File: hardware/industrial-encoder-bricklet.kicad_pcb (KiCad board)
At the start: 2 copper layers, 40 x 40 mm, 67 parts, among them P1 CON-SENSOR, P2 Boot, P3 CONN_8, U1 XMC1XXX24, U2 OPA358, U3 ISL32173E, U4 DRILL, U5 DRILL, U6 DRILL, U7 DRILL

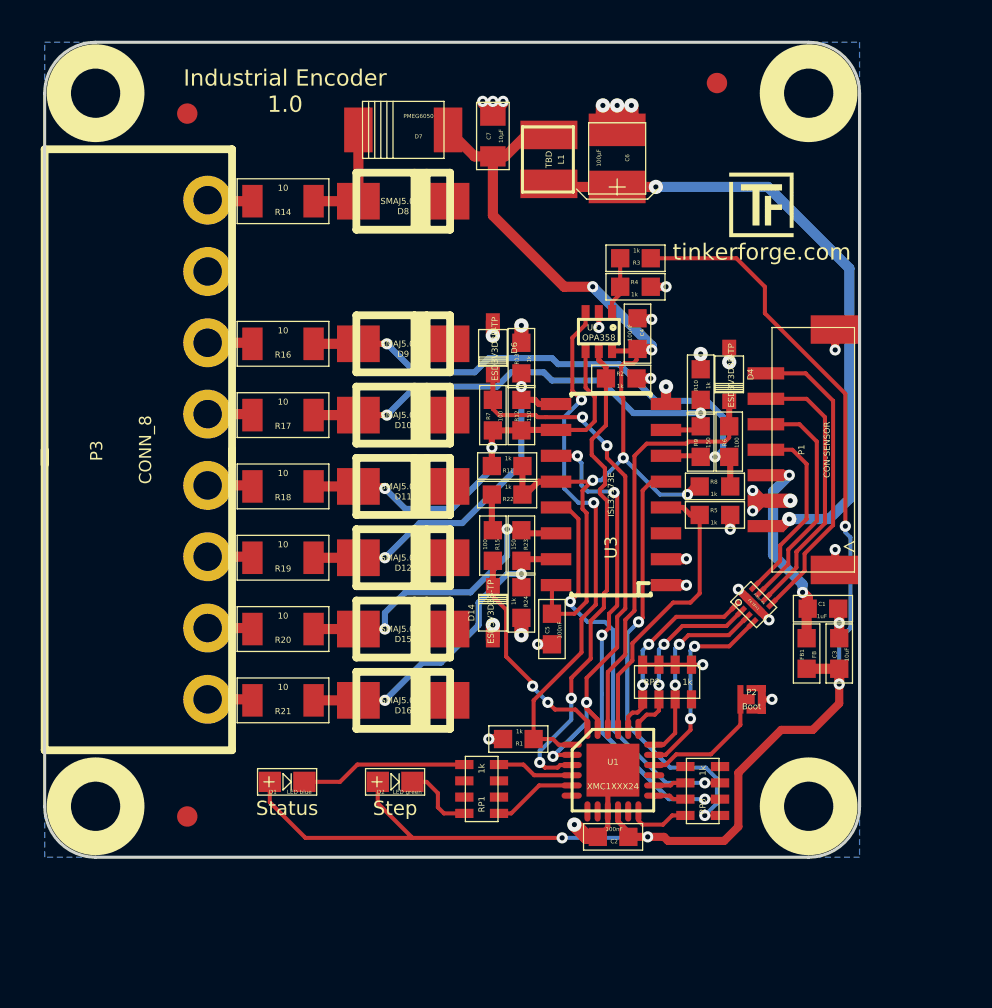
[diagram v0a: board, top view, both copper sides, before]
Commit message: fix filter circuit, not completly finished
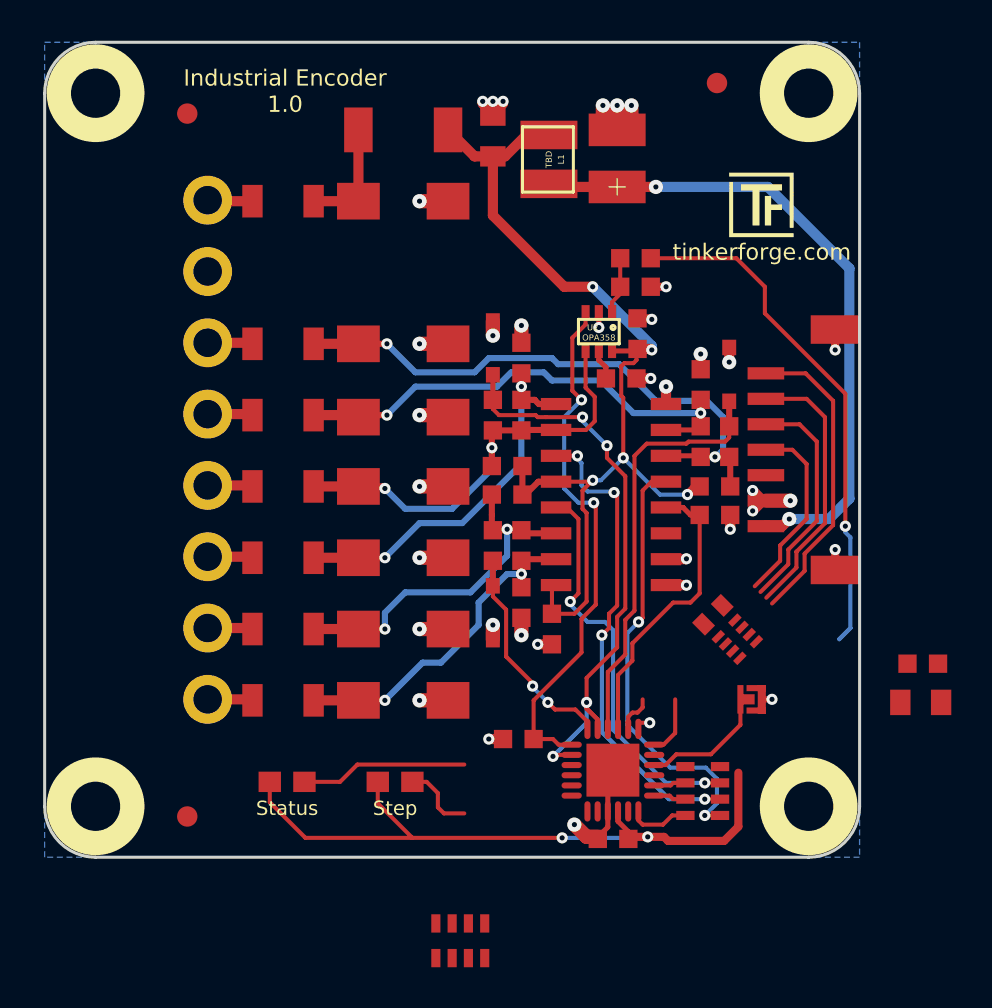
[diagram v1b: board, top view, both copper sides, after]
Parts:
- removed D14: ESD3V3D3B-TP, SOD-323
- removed D15, D16: SMAJ5.0CA, DO-214AC
- removed FB1: FB, kicad-libraries:0603F
- removed FILTER1: Filter-4x, kicad-libraries:DFN8-17x135
- added C8: 10µF, kicad-libraries:C0805, F.Cu at (188.4, 90.5)
- added D13: SMAJ5.0CA, DO-214AC, F.Cu at (184.0, 118.2)
- added D3: ESD3V3D3B-TP, SOD-323, F.Cu at (200.0, 102.2)
- added D5: PMEG6050, SOD-128, F.Cu at (184.0, 90.2)
- C1: value 1uF -> TBD; footprint kicad-libraries:0603F -> kicad-libraries:C0402E
- C2: value 100nF -> 10uF; footprint kicad-libraries:0603F -> kicad-libraries:C0805
- C3: value 10uF -> 100nF; footprint kicad-libraries:0603F -> kicad-libraries:C0603F
- C4: value 100nF -> 1uF; footprint kicad-libraries:0603F -> kicad-libraries:C0603F
- C5: footprint kicad-libraries:0603F -> kicad-libraries:C0603F
- C6: value 100µF -> 100nF; footprint 3528-21 -> kicad-libraries:C0603F
- C7: value 10µF -> 100µF; footprint kicad-libraries:0805 -> 3528-21
- D11: value SMAJ5.0CA -> ESD3V3D3B-TP; footprint DO-214AC -> SOD-323
- D6: value ESD3V3D3B-TP -> SMAJ5.0CA; footprint SOD-323 -> DO-214AC
- D7: value PMEG6050 -> SMAJ5.0CA; footprint SOD-128 -> DO-214AC
- R1, R10, R11, R12, R13, R15, R2, R22, R23, R24, R3, R4, R5, R6, R7, R8, R9: footprint 0603F -> R0603F
- R14, R16, R17, R18, R19, R20, R21: footprint 1206 -> R1206
- RP1: value 1k -> TBD; footprint kicad-libraries:0603X4 -> 4X0402
- RP2: footprint 0603X4 -> kicad-libraries:0603X4
- moved C6 23.3 mm to (191.3, 114.7), turned to 270 degrees
- moved C4 21.4 mm to (209.5, 116.4), turned to 180 degrees
- moved C2 16.5 mm to (209.4, 118.3), turned to 180 degrees
- moved RP2 16.3 mm to (186.8, 130.0)
- moved C5 15.1 mm to (195.5, 100.2), turned to 90 degrees
- moved RP1 14.5 mm to (200.4, 115.2), turned to 135 degrees
- moved C3 14.4 mm to (194.3, 125.0), turned to 0 degrees
- moved D4 11.7 mm to (188.4, 100.9)
- moved D8 10.6 mm to (184.0, 104.3)
- moved D7 10.5 mm to (184.0, 100.7)
- moved D6 8.44 mm to (184.0, 93.7), turned to 0 degrees
- moved D11 7.60 mm to (188.4, 113.9), turned to 90 degrees
- moved D10 7.00 mm to (184.0, 111.2)
- moved D9 7.00 mm to (184.0, 107.7)
- moved C7 6.20 mm to (194.5, 91.6), turned to 90 degrees
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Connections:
- C4 pad 1: +5VA -> GND
- C4 pad 2: GND -> VCC
- C6 pad 1: +5V -> +5VA
- C7 pad 1: GND -> +5V
- C7 pad 2: +5VA -> GND
- D10 pad 1: ~A -> ~B
- D11 pad 1: B/CLK -> GND
- D11 pad 2: GND -> I-T
- D12 pad 1: ~B -> I
- D4 pad 2: A-T -> B-T
- D6 pad 1: GND -> Net-(D5-Pad2)
- D6 pad 2: B-T -> GND
- D7 pad 1: +5VA -> A/DAT
- D7 pad 2: Net-(D7-Pad2) -> GND
- D8 pad 1: Net-(D7-Pad2) -> ~A
- D9 pad 1: A/DAT -> B/CLK
- P1 pad 3: Net-(C1-Pad2) -> VCC
- P1 pad 4: Net-(FILTER1-Pad8) -> Net-(P1-Pad4)
- P1 pad 5: Net-(FILTER1-Pad7) -> Net-(P1-Pad5)
- P1 pad 6: Net-(FILTER1-Pad6) -> Net-(P1-Pad6)
- P1 pad 7: Net-(FILTER1-Pad5) -> Net-(C1-Pad2)
- R14 pad 2: Net-(D7-Pad2) -> Net-(D5-Pad2)
- RP1 pad 1: Net-(D1-Pad2) -> S-CS
- RP1 pad 2: (no net) -> S-CLK
- RP1 pad 3: (no net) -> S-MOSI
- RP1 pad 4: Net-(D2-Pad2) -> S-MISO
- RP1 pad 5: Net-(RP1-Pad5) -> Net-(C1-Pad2)
- RP1 pad 6: (no net) -> Net-(P1-Pad6)
- RP1 pad 7: (no net) -> Net-(P1-Pad5)
- RP1 pad 8: Net-(RP1-Pad8) -> Net-(P1-Pad4)
- RP2 pad 1: GND -> Net-(D1-Pad2)
- RP2 pad 2: GND -> (no net)
- RP2 pad 3: GND -> (no net)
- RP2 pad 4: GND -> Net-(D2-Pad2)
- RP2 pad 5: S-CS -> Net-(RP2-Pad5)
- RP2 pad 6: S-CLK -> (no net)
- RP2 pad 7: S-MOSI -> (no net)
- RP2 pad 8: (no net) -> Net-(RP2-Pad8)
- U1 pad 11: (no net) -> S-CLK
- U1 pad 19: S-CLK -> B-CLK-EN
- U1 pad 3: B-CLK-EN -> (no net)
- U1 pad 4: Net-(RP1-Pad8) -> (no net)
- U1 pad 5: Net-(RP1-Pad5) -> (no net)
- U1 pad 7: (no net) -> Net-(RP2-Pad8)
- U1 pad 8: (no net) -> Net-(RP2-Pad5)
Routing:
- net B-CLK-EN: track 24.3 -> 2.61 mm, vias 2 -> 1
- net Net-(FILTER1-Pad5): track 15.0 -> 0.00 mm
- net Net-(P1-Pad6): track 0.00 -> 13.3 mm
- net Net-(FILTER1-Pad6): track 13.3 -> 0.00 mm
- net VCC: track 72.0 -> 60.1 mm, vias 4 -> 3
- net Net-(P1-Pad5): track 0.00 -> 11.4 mm
- net Net-(FILTER1-Pad7): track 11.4 -> 0.00 mm
- net S-MISO: track 9.80 -> 0.00 mm, vias 2 -> 0
- net S-CLK: track 9.36 -> 0.00 mm, vias 2 -> 0
- net Net-(P1-Pad4): track 0.00 -> 9.34 mm
- net Net-(FILTER1-Pad8): track 9.34 -> 0.00 mm
- net S-CS: track 9.75 -> 1.89 mm, vias 2 -> 0
- net S-MOSI: track 9.57 -> 2.92 mm, vias 2 -> 0
- net GND: track 51.1 -> 44.5 mm, vias 40 -> 36
- net Net-(D7-Pad2): track 5.70 -> 0.00 mm
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
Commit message: schematic fixed
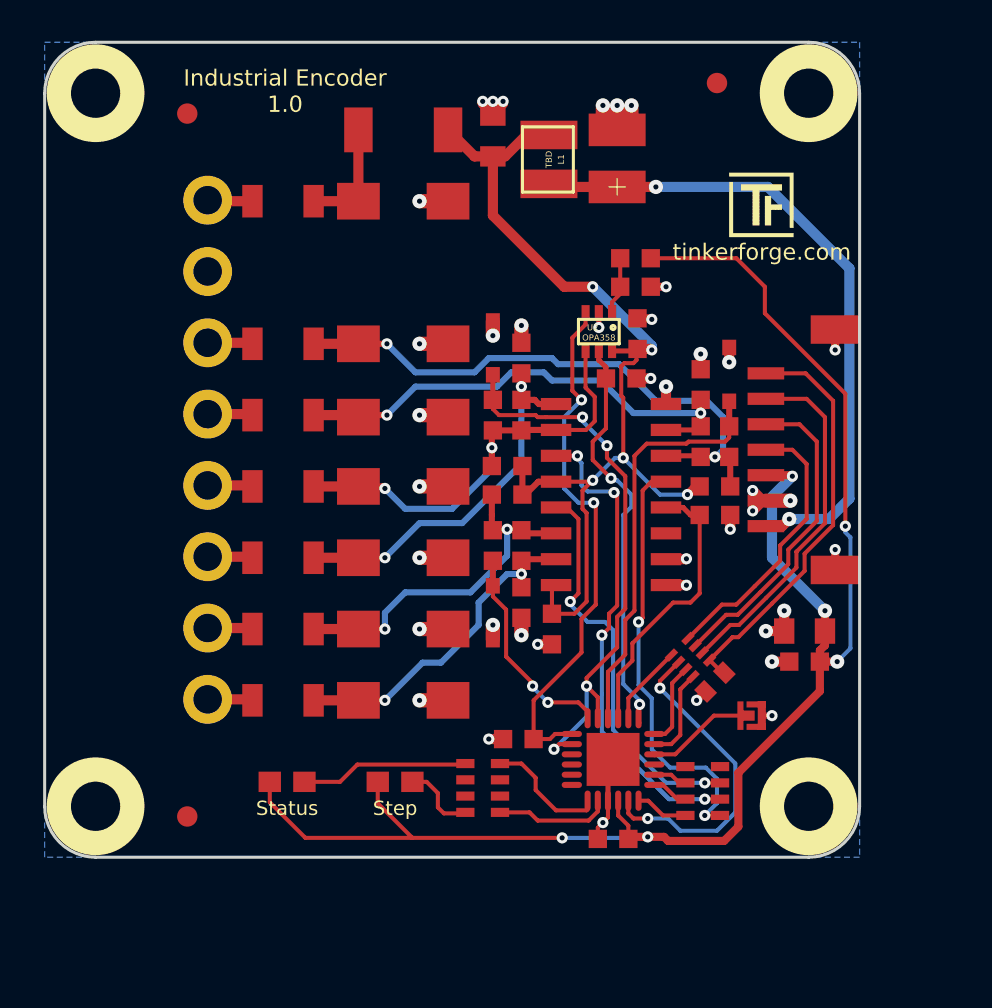
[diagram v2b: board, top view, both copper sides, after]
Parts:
- moved RP2 7.58 mm to (187.9, 122.5), turned to 90 degrees
- moved C2 6.69 mm to (203.7, 114.8), turned to 0 degrees
- moved C4 5.80 mm to (203.7, 116.3), turned to 0 degrees
- moved C1 3.30 mm to (199.3, 117.3), turned to 45 degrees
- moved RP1 2.47 mm to (198.1, 116.1), turned to 315 degrees
- moved P2 0.80 mm to (201.1, 119.0)
- moved U1 0.53 mm to (194.3, 121.1)
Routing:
- net VCC: track 60.1 -> 80.8 mm, vias 3 -> 6
- net B-CLK-EN: track 2.61 -> 19.9 mm, vias 1 -> 2
- net S-CLK: track 0.00 -> 15.9 mm, vias 0 -> 2
- net Net-(RP2-Pad8): track 0.00 -> 6.05 mm
- net Net-(RP2-Pad5): track 0.00 -> 5.68 mm
- net Net-(C1-Pad2): track 15.0 -> 20.2 mm
- net S-MISO: track 0.00 -> 4.58 mm
- net Net-(P1-Pad4): track 9.34 -> 13.7 mm
- net Net-(P1-Pad5): track 11.4 -> 15.7 mm
- net Net-(P1-Pad6): track 13.3 -> 17.6 mm
- net B-T: track 31.3 -> 27.6 mm
- net GND: track 44.5 -> 47.1 mm, vias 36 -> 40
- net S-CS: track 1.89 -> 3.97 mm
- net Net-(P2-Pad2): track 6.70 -> 5.45 mm
- net S-MOSI: track 2.92 -> 4.11 mm
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
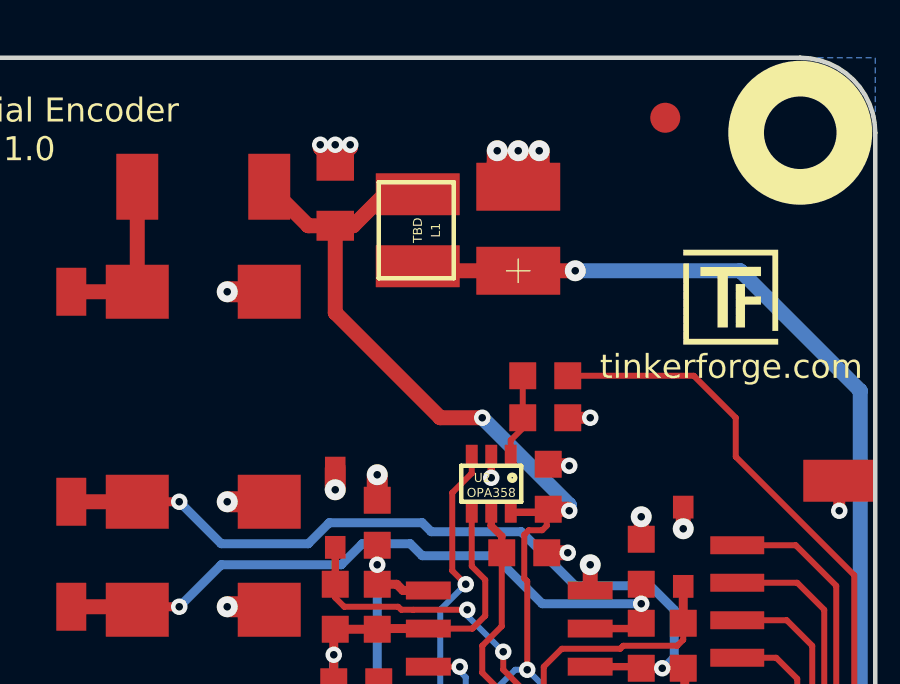
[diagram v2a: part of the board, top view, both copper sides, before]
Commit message: define inductor, update footprints
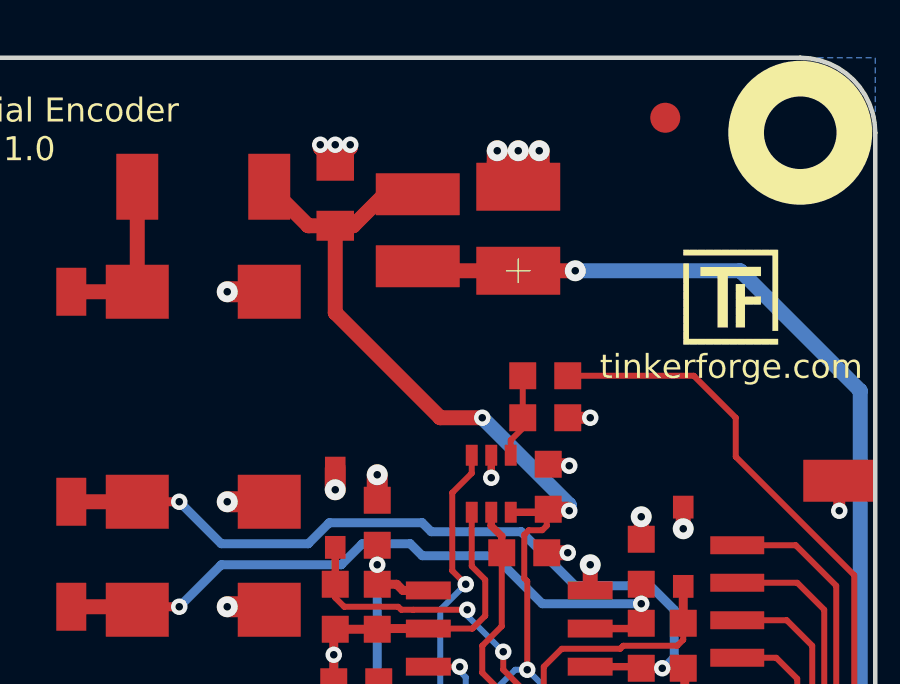
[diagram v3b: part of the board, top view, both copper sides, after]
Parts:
- L1: value TBD -> 6.8uH
- U2: footprint SC70-6 -> kicad-libraries:SC70-6
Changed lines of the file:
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@@
-(kicad_pcb (version 4) (host pcbnew 4.0.2+e4-6225~38~ubuntu15.10.1-stable)
+(kicad_pcb (version 4) (host pcbnew 4.0.6-e0-6349~53~ubuntu16.04.1)
   (general
     (links 132)
     (no_connects 0)
-    (area 166.324999 85.824999 206.475001 125.975001)
+    (area 165.544999 85.044999 276.69286 162.45)
     (thickness 1.6)
     (drawings 21)
@@
       (xy 3.1242 3.1242)) (layer F.SilkS) (width 0.00254))
   )
-  (module kicad-libraries:WE-LQ-1210 (layer F.Cu)
-    (at 191.15 91.65 90)
-    (fp_text reference L1 (at 0 0.6 90) (layer F.SilkS)
-      (effects (font (size 0.3 0.3) (thickness 0.075)))
-    )
-    (fp_text value TBD (at 0 0 90) (layer F.SilkS)
-      (effects (font (size 0.3 0.3) (thickness 0.075)))
-    )
-    (fp_line (start -1.6 -1.3) (end 1.6 -1.3) (layer F.SilkS) (width 0.15))
-    (fp_line (start 1.6 -1.3) (end 1.6 1.2) (layer F.SilkS) (width 0.15))
-    (fp_line (start 1.6 1.2) (end -1.6 1.2) (layer F.SilkS) (width 0.15))
-    (fp_line (start -1.6 1.2) (end -1.6 -1.3) (layer F.SilkS) (width 0.15))
-    (pad 1 smd rect (at -1.2 0 90) (size 1.4 2.8) (layers F.Cu F.Paste F.Mask)
-      (net 8 +5V))
-    (pad 2 smd rect (at 1.2 0 90) (size 1.4 2.8) (layers F.Cu F.Paste F.Mask)
-      (net 7 +5VA))
-  )
   (module kicad-libraries:DRILL_NP (layer F.Cu)
     (at 168.9 88.4)
@@
     )
   )
-  (module SC70-6 (layer F.Cu)
-    (at 193.6 100.1 180)
-    (fp_text reference U2 (at 0.3 0.2 180) (layer F.SilkS)
-      (effects (font (size 0.3 0.3) (thickness 0.075)))
-    )
-    (fp_text value OPA358 (at 0 -0.3 180) (layer F.SilkS)
-      (effects (font (size 0.3 0.3) (thickness 0.075)))
-    )
-    (fp_circle (center -0.7 0.2) (end -0.7 0.3) (layer F.SilkS) (width 0.15))
-    (fp_line (start -1 -0.6) (end 1 -0.6) (layer F.SilkS) (width 0.15))
-    (fp_line (start 1 -0.6) (end 1 0.6) (layer F.SilkS) (width 0.15))
-    (fp_line (start 1 0.6) (end -1 0.6) (layer F.SilkS) (width 0.15))
-    (fp_line (start -1 0.6) (end -1 -0.6) (layer F.SilkS) (width 0.15))
-    (pad 1 smd rect (at -0.65 0.95 180) (size 0.4 0.7) (layers F.Cu F.Paste F.Mask)
-      (net 25 "Net-(R3-Pad1)"))
-    (pad 2 smd rect (at 0 0.95 180) (size 0.4 0.7) (layers F.Cu F.Paste F.Mask)
-      (net 1 GND))
-    (pad 3 smd rect (at 0.65 0.95 180) (size 0.4 0.7) (layers F.Cu F.Paste F.Mask)
-      (net 28 B-CLK))
-    (pad 4 smd rect (at 0.65 -0.95 180) (size 0.4 0.7) (layers F.Cu F.Paste F.Mask)
-      (net 13 B/CLK))
-    (pad 6 smd rect (at -0.65 -0.95 180) (size 0.4 0.7) (layers F.Cu F.Paste F.Mask)
-      (net 7 +5VA))
-    (pad 5 smd rect (at 0 -0.95 180) (size 0.4 0.7) (layers F.Cu F.Paste F.Mask)
-      (net 29 B-CLK-EN))
-  )
   (module SOIC16 (layer F.Cu)
     (at 194.2 108.1 90)
@@
     )
   )
+  (module kicad-libraries:WE-LQ-1210 (layer F.Cu)
+    (at 191.15 91.65 90)
+    (fp_text reference L1 (at 0 0.6 90) (layer F.Fab)
+      (effects (font (size 0.3 0.3) (thickness 0.075)))
+    )
+    (fp_text value 6.8uH (at 0 0 90) (layer F.Fab)
+      (effects (font (size 0.3 0.3) (thickness 0.075)))
+    )
+    (fp_line (start -1.6 -1.3) (end 1.6 -1.3) (layer F.Fab) (width 0.15))
+    (fp_line (start 1.6 -1.3) (end 1.6 1.2) (layer F.Fab) (width 0.15))
+    (fp_line (start 1.6 1.2) (end -1.6 1.2) (layer F.Fab) (width 0.15))
+    (fp_line (start -1.6 1.2) (end -1.6 -1.3) (layer F.Fab) (width 0.15))
+    (pad 1 smd rect (at -1.2 0 90) (size 1.4 2.8) (layers F.Cu F.Paste F.Mask)
+      (net 8 +5V))
+    (pad 2 smd rect (at 1.2 0 90) (size 1.4 2.8) (layers F.Cu F.Paste F.Mask)
+      (net 7 +5VA))
+  )
+  (module kicad-libraries:SC70-6 (layer F.Cu)
+    (at 193.6 100.1 180)
+    (fp_text reference U2 (at 0.3 0.2 180) (layer F.Fab)
+      (effects (font (size 0.3 0.3) (thickness 0.075)))
+    )
+    (fp_text value OPA358 (at 0 -0.3 180) (layer F.Fab)
+      (effects (font (size 0.3 0.3) (thickness 0.075)))
+    )
+    (fp_circle (center -0.7 0.2) (end -0.7 0.3) (layer F.Fab) (width 0.15))
+    (fp_line (start -1 -0.6) (end 1 -0.6) (layer F.Fab) (width 0.15))
+    (fp_line (start 1 -0.6) (end 1 0.6) (layer F.Fab) (width 0.15))
+    (fp_line (start 1 0.6) (end -1 0.6) (layer F.Fab) (width 0.15))
+    (fp_line (start -1 0.6) (end -1 -0.6) (layer F.Fab) (width 0.15))
+    (pad 1 smd rect (at -0.65 0.95 180) (size 0.4 0.7) (layers F.Cu F.Paste F.Mask)
+      (net 25 "Net-(R3-Pad1)"))
+    (pad 2 smd rect (at 0 0.95 180) (size 0.4 0.7) (layers F.Cu F.Paste F.Mask)
+      (net 1 GND))
+    (pad 3 smd rect (at 0.65 0.95 180) (size 0.4 0.7) (layers F.Cu F.Paste F.Mask)
+      (net 28 B-CLK))
+    (pad 4 smd rect (at 0.65 -0.95 180) (size 0.4 0.7) (layers F.Cu F.Paste F.Mask)
+      (net 13 B/CLK))
+    (pad 6 smd rect (at -0.65 -0.95 180) (size 0.4 0.7) (layers F.Cu F.Paste F.Mask)
+      (net 7 +5VA))
+    (pad 5 smd rect (at 0 -0.95 180) (size 0.4 0.7) (layers F.Cu F.Paste F.Mask)
+      (net 29 B-CLK-EN))
+  )
   (gr_text "Copyright Tinkerforge GmbH 2017.\nThis documentation describes Open Hardware and is licensed under the\nCERN OHL v. 1.1.\nYou may redistribute and modify this documentation under the terms of the\nCERN OHL v.1.1. (http://ohwr.org/cernohl). This documentation is distributed\nWITHOUT ANY EXPRESS OR IMPLIED WARRANTY, INCLUDING OF\nMERCHANTABILITY, SATISFACTORY QUALITY AND FITNESS FOR A\nPARTICULAR PURPOSE. Please see the CERN OHL v.1.1 for applicable\nconditions" (at 231.8 150.9) (layer Cmts.User)
